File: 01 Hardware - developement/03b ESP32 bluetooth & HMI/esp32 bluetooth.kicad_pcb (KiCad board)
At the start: 2 copper layers, 152.4 x 142.2 mm, 115 parts, among them J1 I2C, J2 UART, J3 power supply, J4 Jtag, J5 I2S, J6 Backlight and leds, J7 to stepper motor, J8 Conn_01x01_Pin, Q1 BC817, Q2 BSS138, Q3 BSS138, Q4 BSS138, SW1 SW_Push_Dual, SW10 Strapping button, SW2 SW_Push_Dual, SW3 SW_Push_Dual, SW4 SW_Push_Dual, SW5 SW_Push_Dual, SW6 Rotary_Encoder_Switch, SW7 Rotary_Encoder_Switch, SW8 Strapping button, SW9 Strapping button, U1 DRV8825_STEPPER_MOTOR_DRIVER_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, U2 ESP32-DevKitC, U3 MCP23008

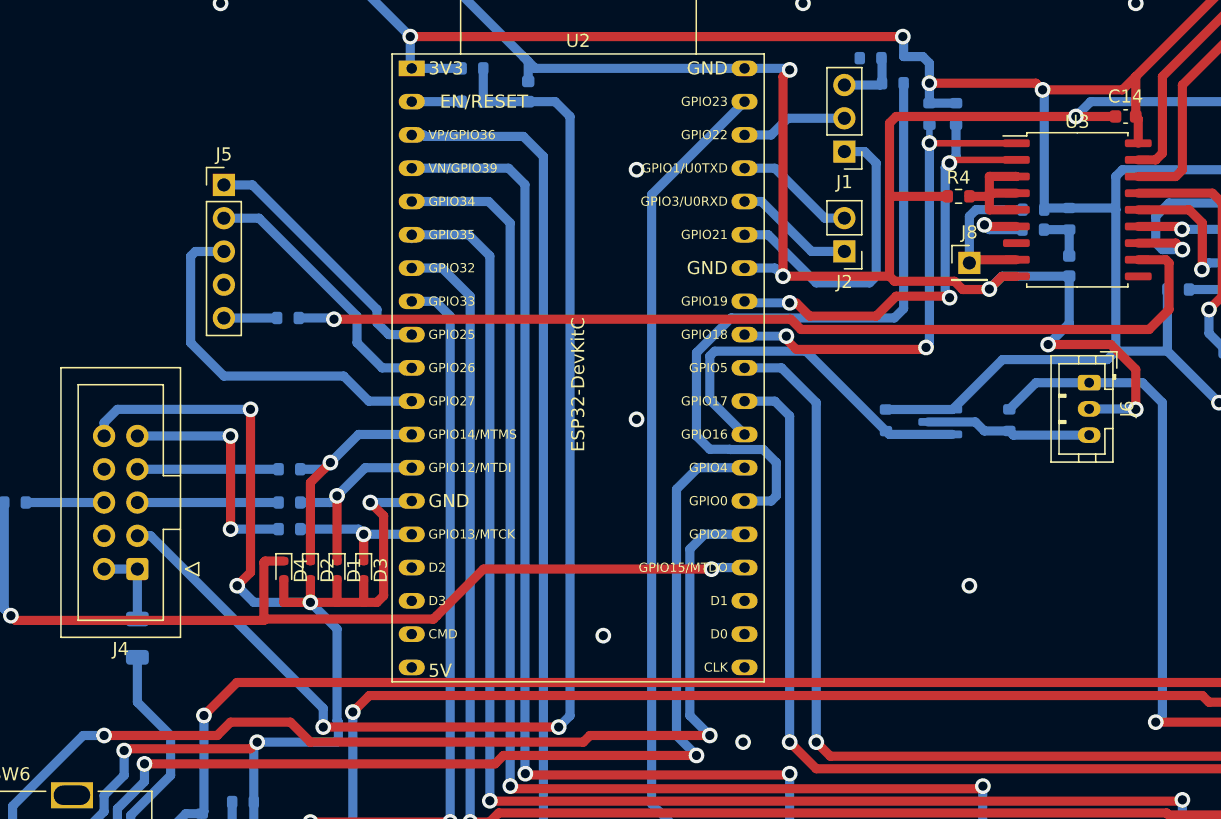
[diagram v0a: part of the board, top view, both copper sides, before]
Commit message: taki backup, że po dodaniu DRAM_INT działa program, ale błąd występuje - POWRÓT DO WERSJI
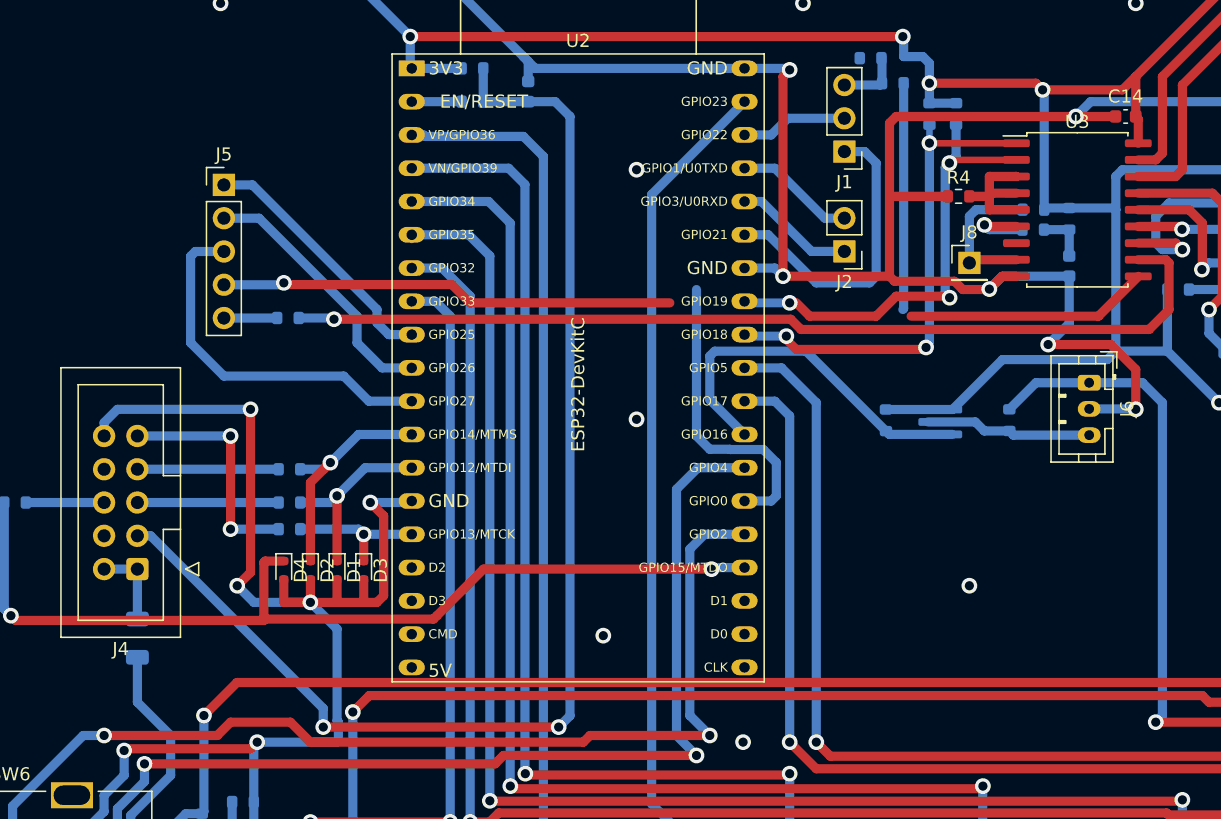
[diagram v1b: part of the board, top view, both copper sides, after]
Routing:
- net unconnected-(J5-Pin_4-Pad4): track 0.20 -> 34.9 mm, vias 0 -> 1
- net unconnected-(U3-GP0-Pad10): track 0.00 -> 18.6 mm
- net /BOOT: track 52.8 -> 40.5 mm

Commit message: nie wiem czy to zadziała jest zbuggowana syncgronizacja wysyłania i2c ESP32
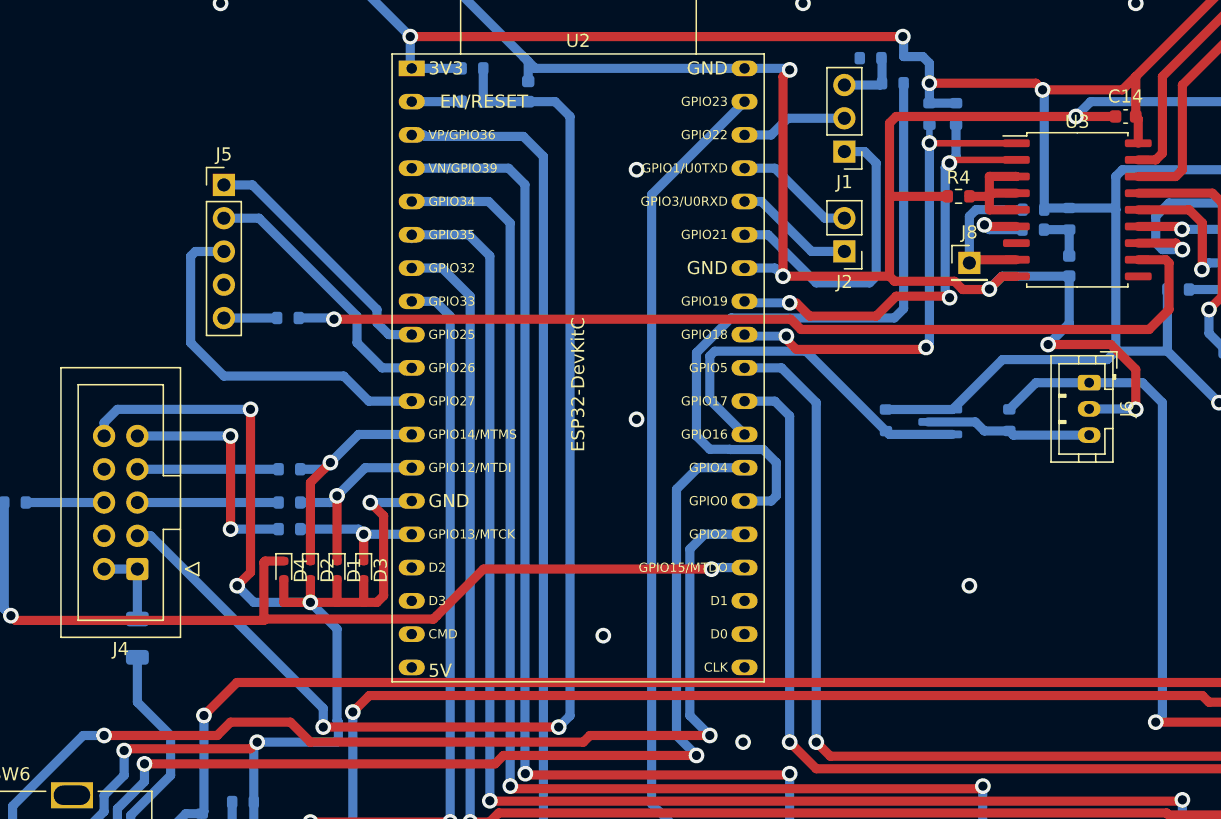
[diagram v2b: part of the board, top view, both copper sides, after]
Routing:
- net unconnected-(J5-Pin_4-Pad4): track 34.9 -> 0.20 mm, vias 1 -> 0
- net unconnected-(U3-GP0-Pad10): track 18.6 -> 0.00 mm
- net /BOOT: track 40.5 -> 52.8 mm
